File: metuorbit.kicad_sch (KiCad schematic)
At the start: 0 parts

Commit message: Boards are added for library and simple connections are made.
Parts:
- added IC1: BLACKPILLF4, Black Pill:BLACKPILLF4, symbol Black Pill:BLACKPILLF4
- added IC2: LoRa E220-900T30D, E220-900T30D:MESHNODES-E220-900T30D+22D, symbol LocalSymbols:E220-900T30D
- added IC3: BNO055, Boards:BNO055, symbol LocalSymbols:BNO055_Module
- added IC4: NEO-M8N, Boards:NEO-M8N, symbol LocalSymbols:NEO-M8N
- added IC5: BMP388, Boards:BMP388, symbol LocalSymbols:BMP388
- added IC6: MicroSD_Reader, Boards:MicroSD Reader, symbol LocalSymbols:MicroSD_Reader
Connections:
- new net +3V3: IC1.3V3_1 (3V3), IC3.1 (VIN), IC4.4 (VCC), IC5.1 (VCC), IC6.2 (VCC)
- new net BMP_SCL: IC1.PA8, IC5.4 (SCL)
- new net BMP_SDA: IC1.PB4, IC5.6 (SDA)
- new net BNO_SCL: IC1.PB10, IC3.5 (SCL)
- new net BNO_SDA: IC1.PB3, IC3.4 (SDA)
- new net GND: IC1.GND_1 (GND), IC1.GND_3 (GND), IC3.3 (GND), IC4.1 (GND), IC5.3 (GND), IC5.5 (SDO), IC6.1 (GND)
- new net NEO_RX: IC1.PA2, IC4.3 (RX)
- new net NEO_TX: IC1.PA3, IC4.2 (TX)
- new net SD_CS: IC1.PA4, IC6.6 (CS)
- new net SD_MISO: IC1.PA6, IC6.3 (MISO)
- new net SD_MOSI: IC1.PA7, IC6.4 (MOSI)
- new net SD_SCK: IC1.PA5, IC6.5 (SCK)
- no-connect marks 0 -> 9
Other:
- title: (none) -> METUORBIT PCB Schematic

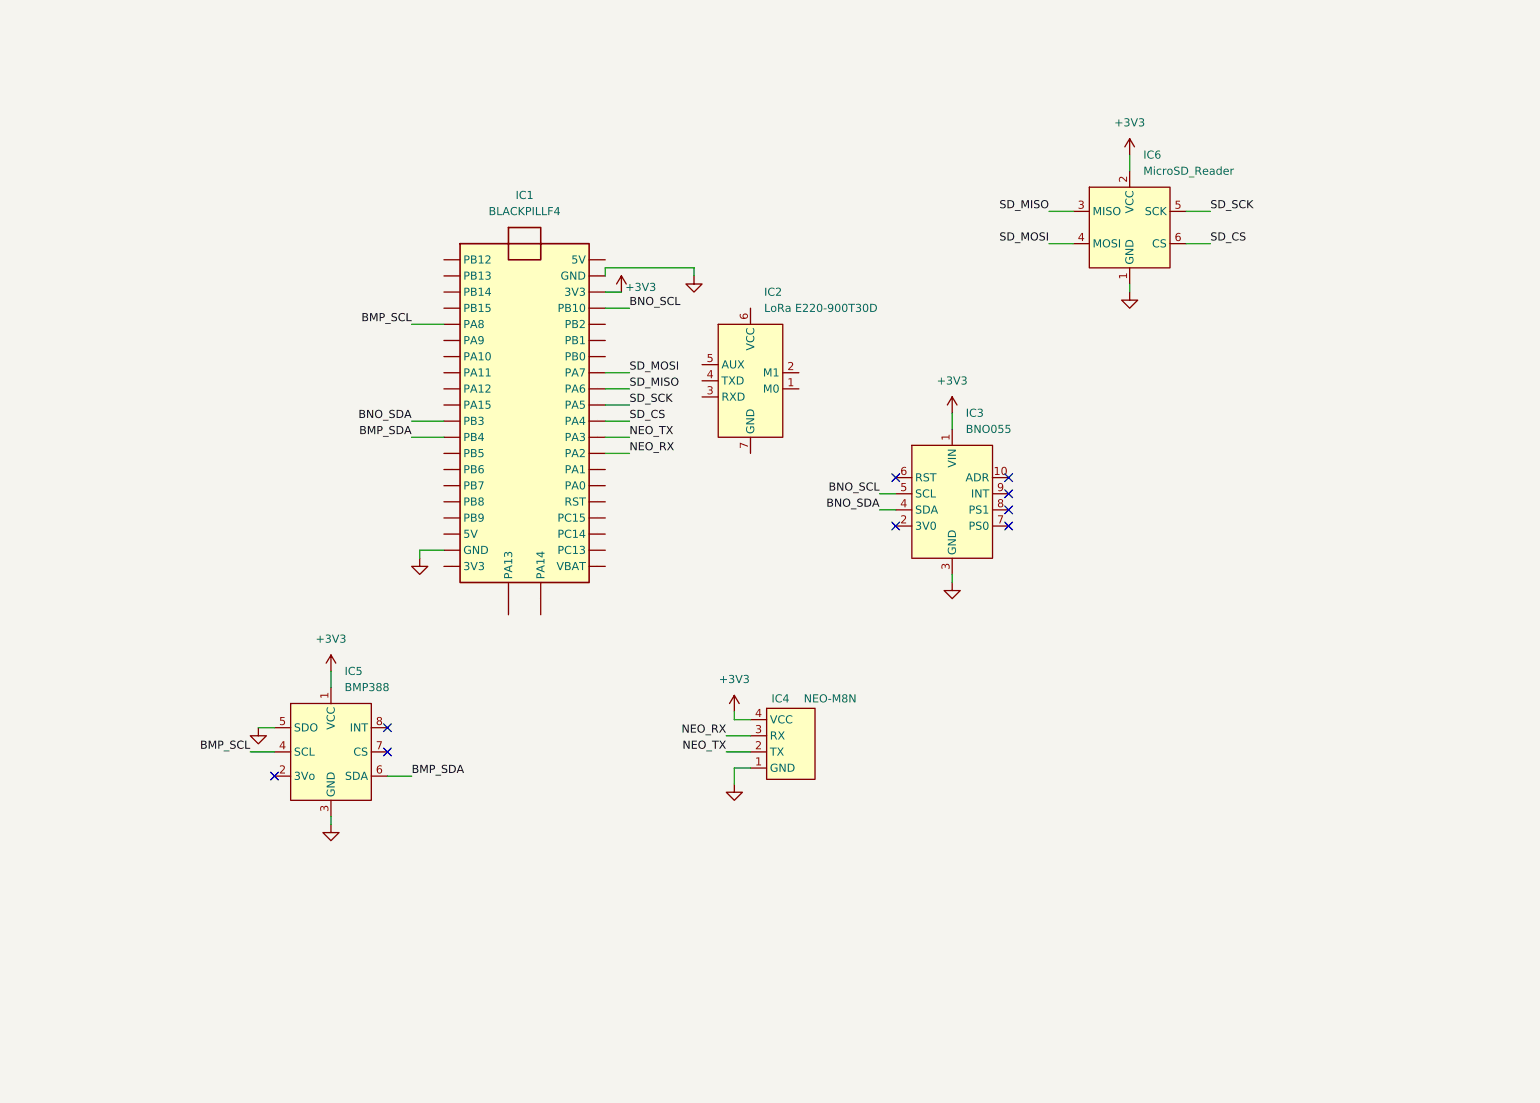
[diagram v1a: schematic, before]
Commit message: Power regulators and output pins are added.
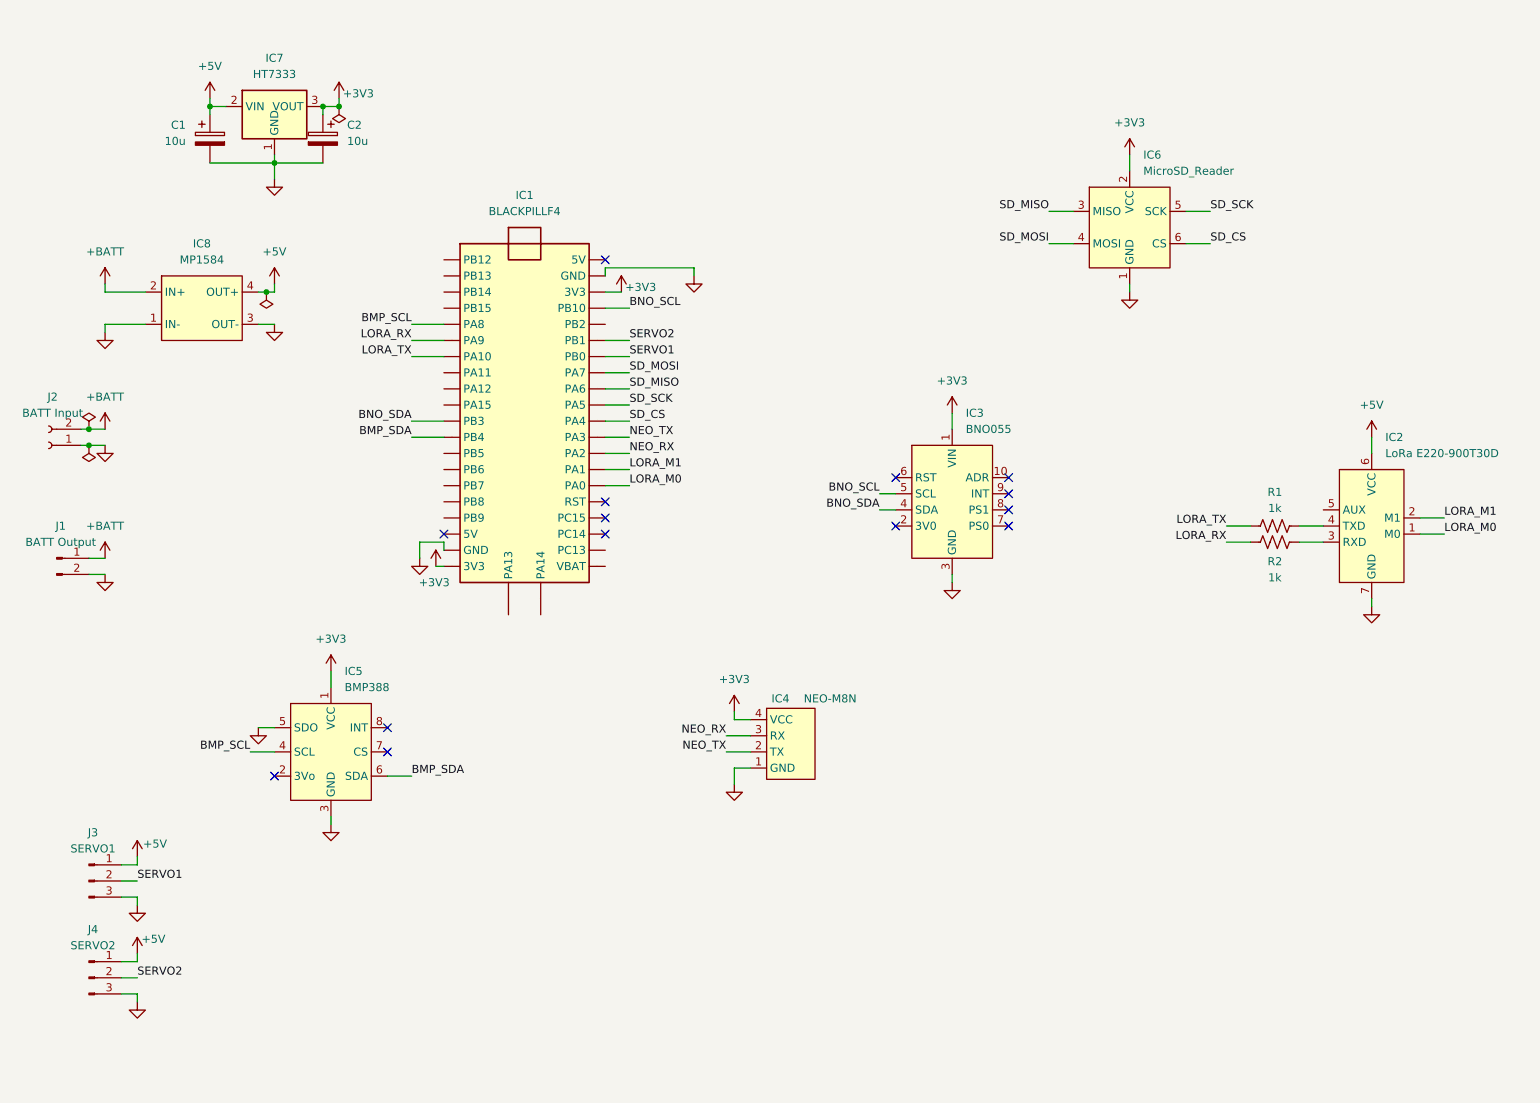
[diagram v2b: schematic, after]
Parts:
- added C1, C2: 10u, Capacitor_THT:CP_Radial_D5.0mm_P2.50mm, symbol Device:C_Polarized
- added IC7: HT7333, Package_TO_SOT_THT:TO-92, symbol Regulator_Linear:HT75xx-1-SOT89
- added IC8: MP1584, Boards:MP1584, symbol LocalSymbols:MP1584
- added J1: BATT Output, Connector_Wire:SolderWire-4sqmm_1x02_P12mm_D3mm_OD6mm, symbol Connector:Conn_01x02_Pin
- added J2: BATT Input, Connector_AMASS:AMASS_XT60-F_1x02_P7.20mm_Vertical, symbol Connector:Conn_01x02_Socket
- added J3: SERVO1, symbol Connector:Conn_01x03_Pin
- added J4: SERVO2, symbol Connector:Conn_01x03_Pin
- added R1, R2: 1k, Resistor_THT:R_Axial_DIN0207_L6.3mm_D2.5mm_P10.16mm_Horizontal, symbol Device:R_US
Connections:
- net +3V3: now also IC1.3V3_2 (3V3), C2.1, IC7.3 (VOUT)
- net GND: now also IC2.7 (GND), C1.2, C2.2, IC7.1 (GND), IC8.1 (IN-), IC8.3 (OUT-), J1.2 (Pin_2), J2.1 (Pin_1), J3.3 (Pin_3), J4.3 (Pin_3)
- net LORA_M0: now reaches IC2.1 (M0)
- net LORA_M0: now also IC1.PA0
- net LORA_M1: now reaches IC2.2 (M1)
- net LORA_M1: now also IC1.PA1
- net at IC2.3 (RXD): now also R2.2
- net at IC2.4 (TXD): now also R1.2
- net +5V: now reaches IC2.6 (VCC)
- net +5V: now also C1.1, IC7.2 (VIN), IC8.4 (OUT+), J3.1 (Pin_1), J4.1 (Pin_1)
- net LORA_TX: now reaches IC1.PA10
- net LORA_TX: now also R1.1
- net LORA_RX: now reaches IC1.PA9
- net LORA_RX: now also R2.1
- net SERVO1: now reaches IC1.PB0
- net SERVO1: now also J3.2 (Pin_2)
- net SERVO2: now reaches IC1.PB1
- net SERVO2: now also J4.2 (Pin_2)
- new net +BATT: IC8.2 (IN+), J1.1 (Pin_1), J2.2 (Pin_2)
- no-connect marks 9 -> 14
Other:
- moved on the sheet: IC2

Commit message: General layout in pcb is determined.
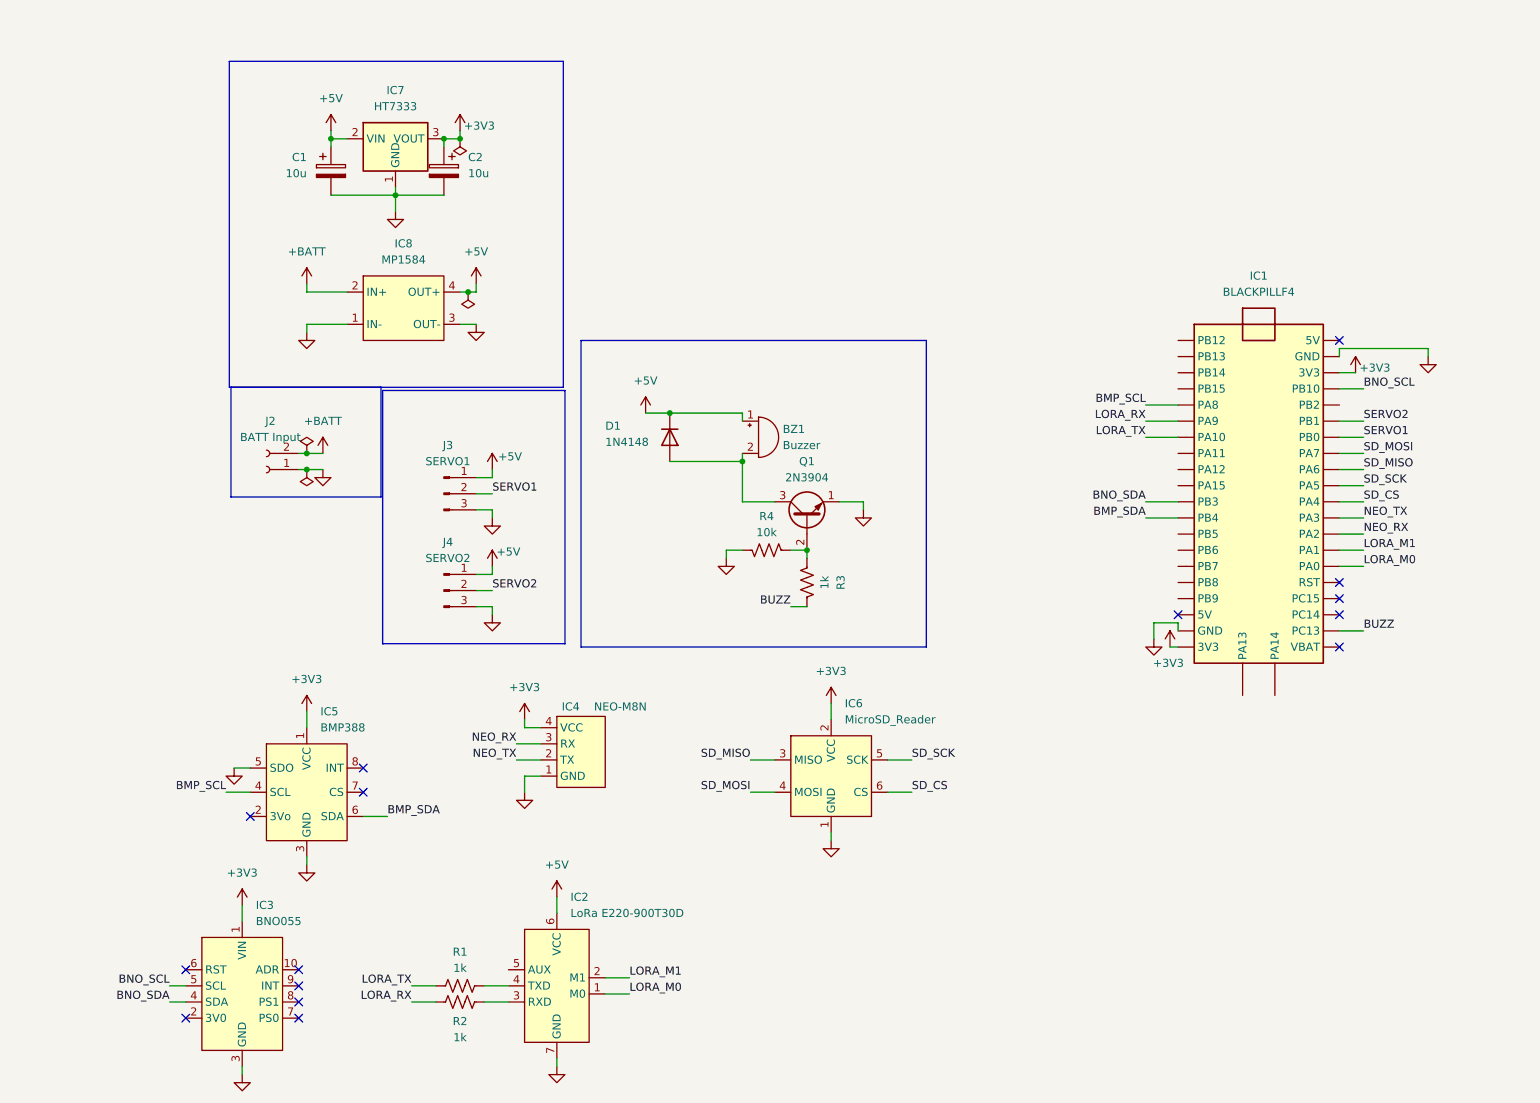
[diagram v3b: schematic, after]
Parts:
- removed J1: BATT Output, Connector_Wire:SolderWire-4sqmm_1x02_P12mm_D3mm_OD6mm, symbol Connector:Conn_01x02_Pin
- added BZ1: Buzzer, Buzzer_Beeper:Buzzer_12x9.5RM7.6, symbol Device:Buzzer
- added D1: 1N4148, Diode_THT:D_DO-35_SOD27_P7.62mm_Horizontal, symbol Diode:1N4148
- added Q1: 2N3904, Package_TO_SOT_THT:TO-92_Inline, symbol Transistor_BJT:2N3904
- added R3: 1k, Resistor_THT:R_Axial_DIN0207_L6.3mm_D2.5mm_P10.16mm_Horizontal, symbol Device:R_US
- added R4: 10k, Resistor_THT:R_Axial_DIN0207_L6.3mm_D2.5mm_P10.16mm_Horizontal, symbol Device:R_US
- J2: footprint Connector_AMASS:AMASS_XT60-F_1x02_P7.20mm_Vertical -> Connector_Wire:SolderWire-6sqmm_1x02_P14mm_D3.5mm_OD7mm
- J3, J4: footprint (none) -> Connector_PinHeader_2.54mm:PinHeader_1x03_P2.54mm_Vertical
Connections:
- net +5V: now also BZ1.1 (+), D1.1 (K)
- net GND: now also Q1.1 (E), R4.2
- net BUZZ: now reaches IC1.PC13
- net BUZZ: now also R3.1
- new net: BZ1.2 (-), D1.2 (A), Q1.3 (C)
- new net: Q1.2 (B), R3.2, R4.1
- no-connect marks 14 -> 15
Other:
- moved on the sheet: C1, C2, IC1, IC2, IC3, IC4, IC5, IC6, IC7, IC8, J2, J3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

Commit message: Resistors are changed to SMD, Schematic is organized.
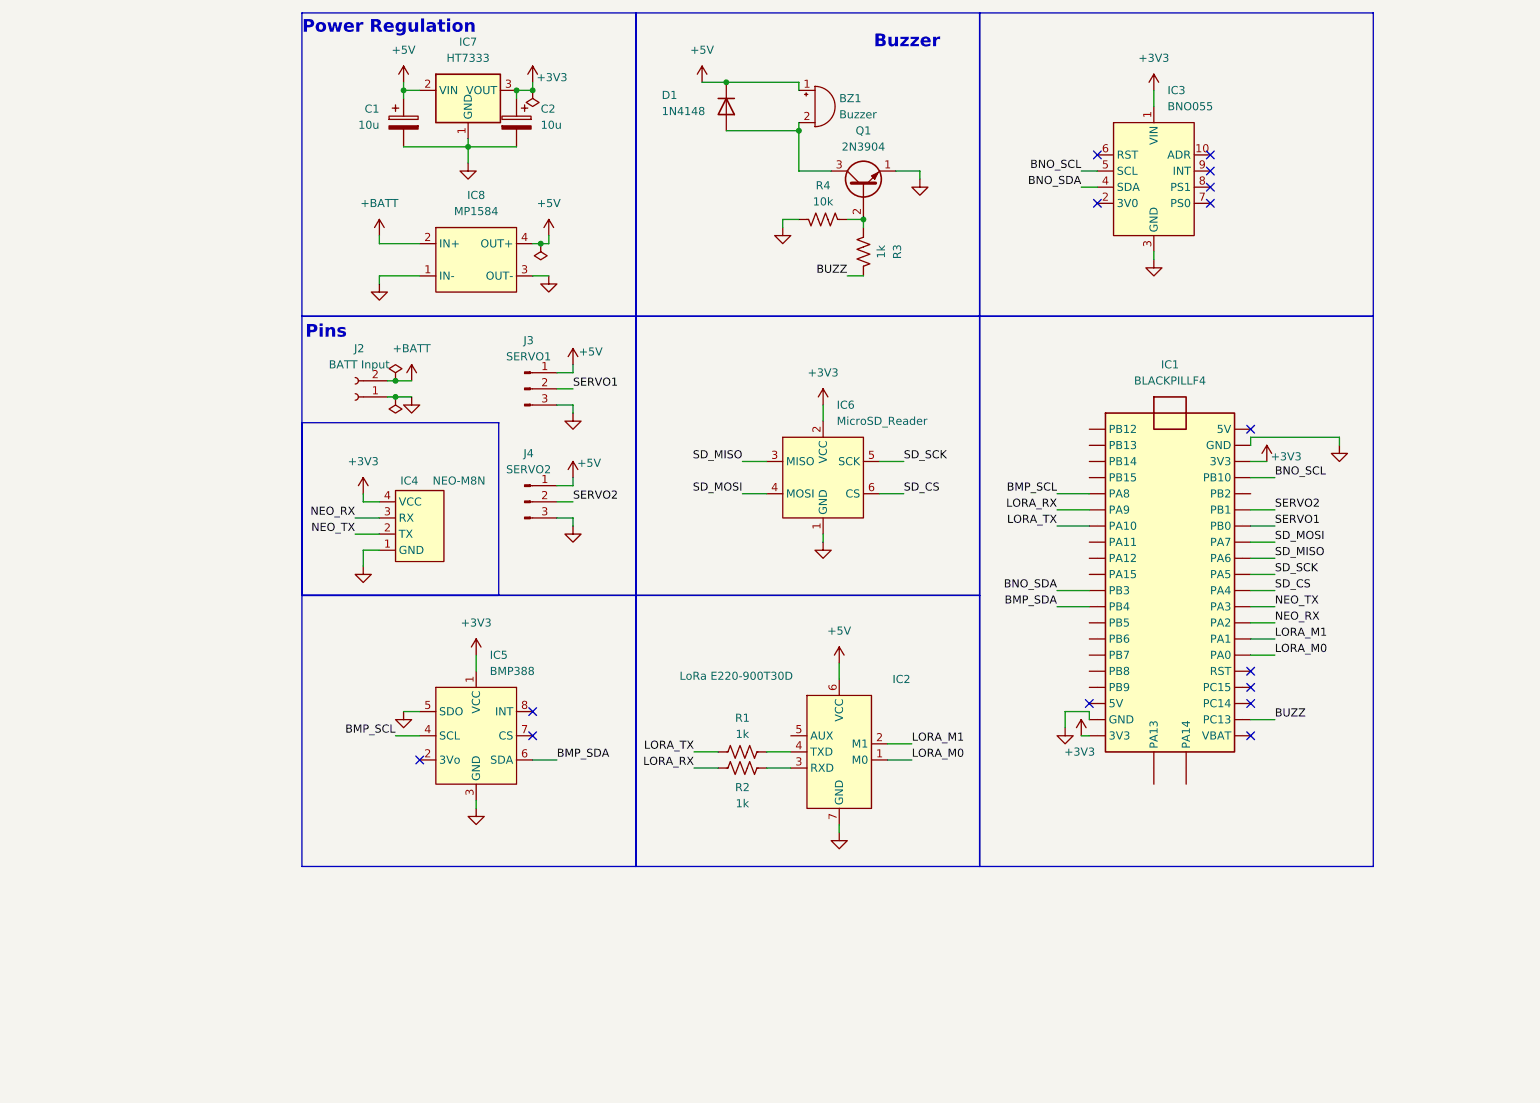
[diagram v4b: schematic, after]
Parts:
- R1, R2, R3, R4: footprint Resistor_THT:R_Axial_DIN0207_L6.3mm_D2.5mm_P10.16mm_Horizontal -> Resistor_SMD:R_1206_3216Metric_Pad1.30x1.75mm_HandSolder
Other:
- note added: "Buzzer"
- note added: "Pins"
- note added: "Power Regulation"
- moved on the sheet: BZ1, C1, C2, D1, IC1, IC2, IC3, IC4, IC5, IC6, IC7, IC8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
